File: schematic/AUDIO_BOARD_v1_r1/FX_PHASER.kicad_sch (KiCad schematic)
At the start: 43 parts, among them U50 LM13700, U51 LM13700, U52 OPA1678, U53 OPA1678, U54 OPA1678

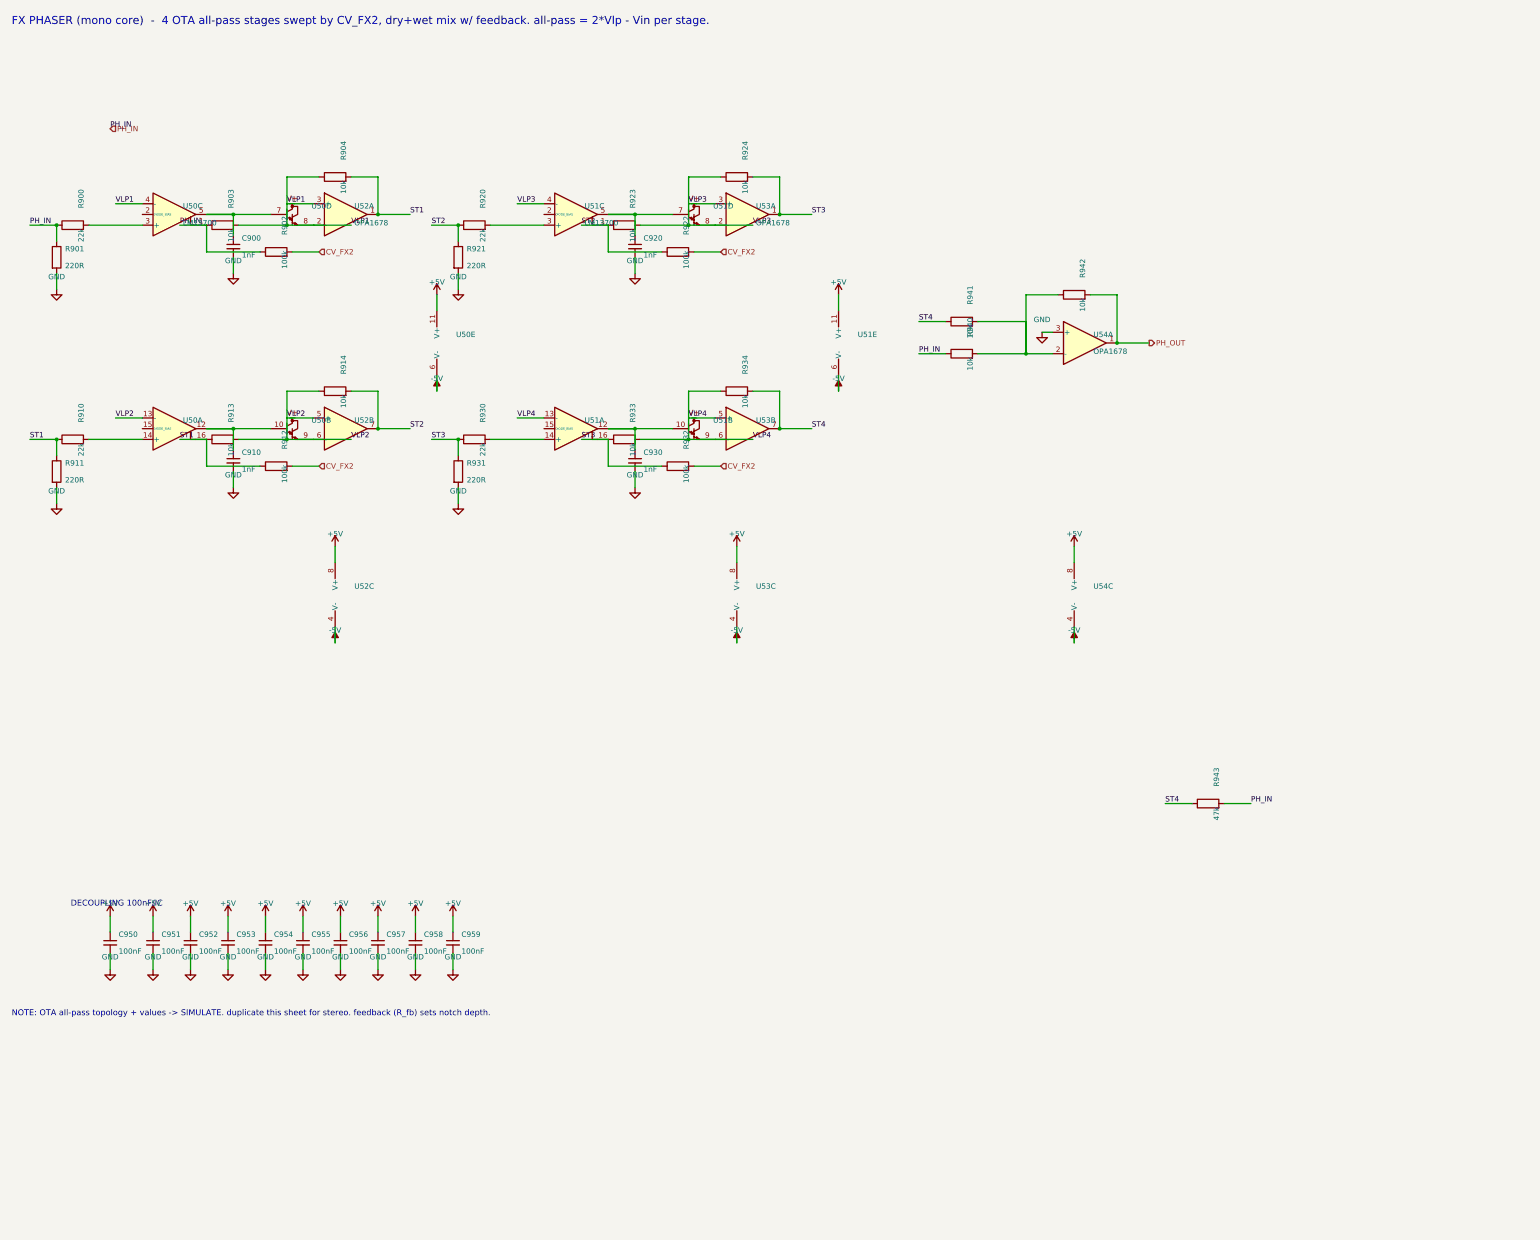
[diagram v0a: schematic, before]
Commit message: readme, audio board schematic stuff
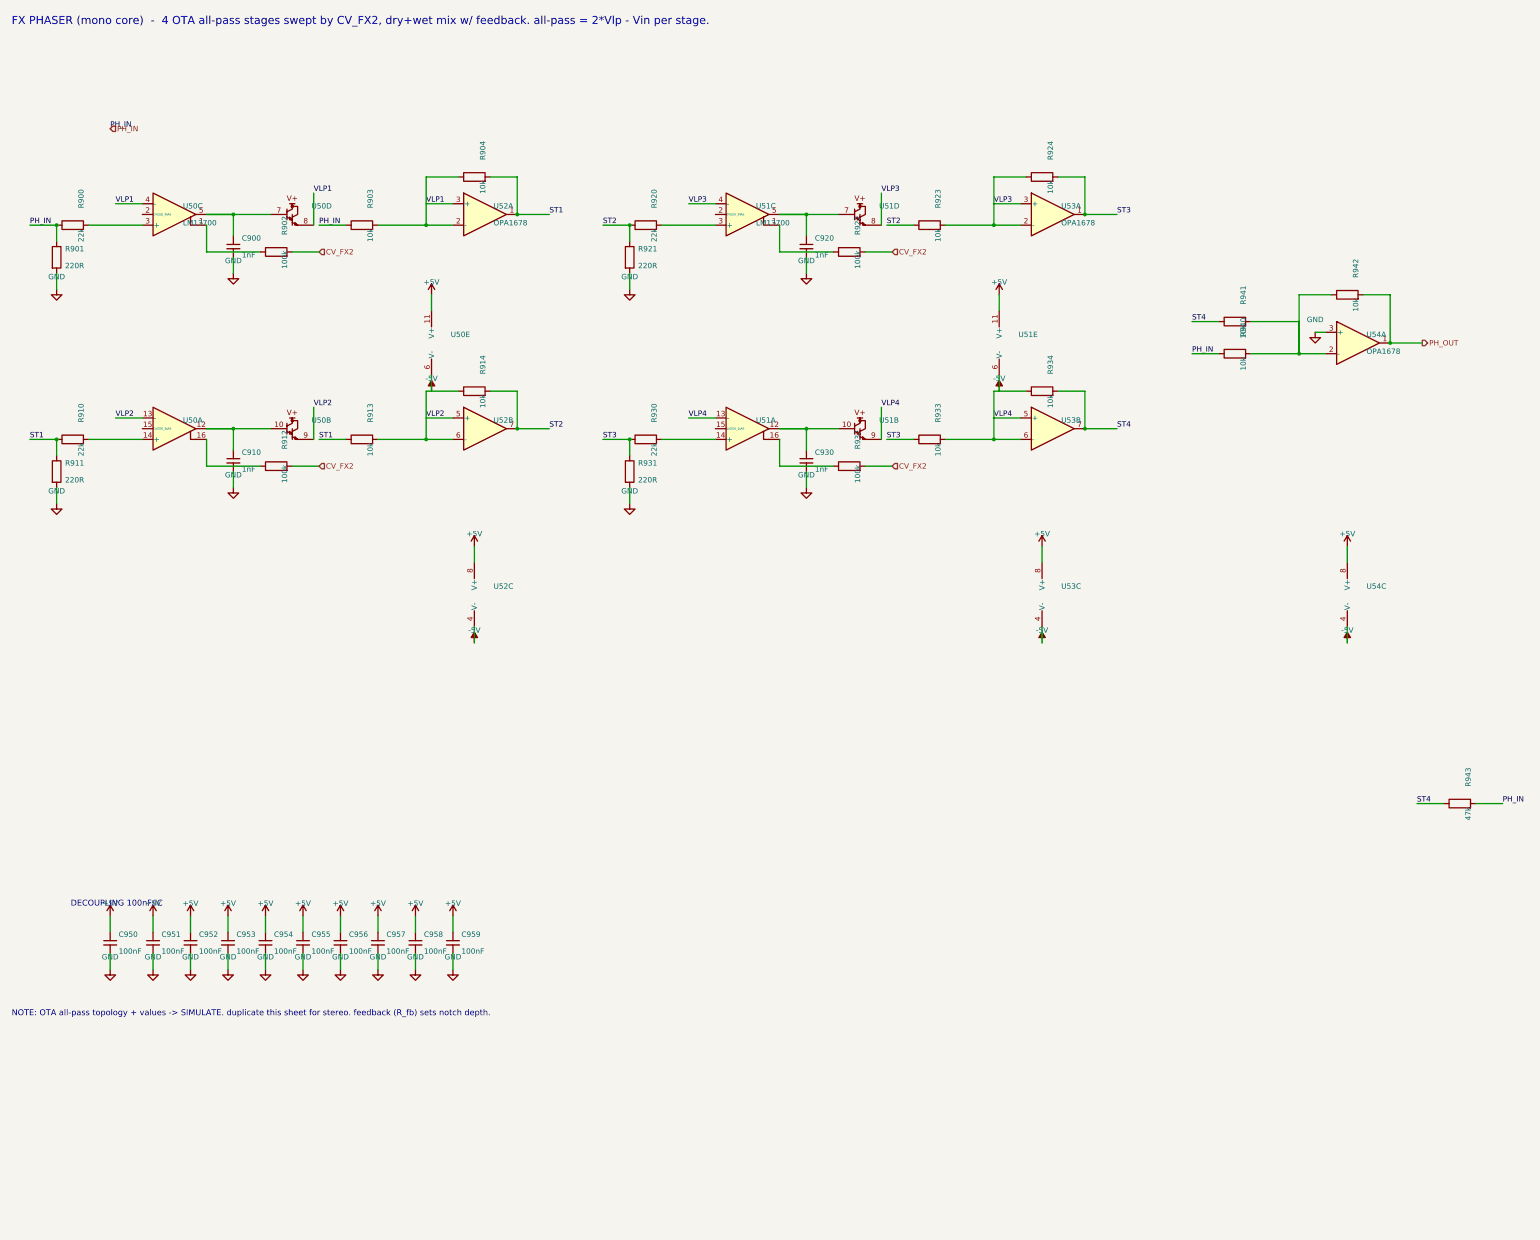
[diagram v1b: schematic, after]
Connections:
- net PH_IN: no longer R902.1, U50.1
- net ST1: no longer R912.1, U50.16
- net ST2: no longer R922.1, U51.1
- net ST3: no longer R932.1, U51.16
- new net: R902.1, U50.1
- new net: R912.1, U50.16
- new net: R932.1, U51.16
- new net: R922.1, U51.1

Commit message: phaser? schematic is messy
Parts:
- removed C900, C920: 1nF, Capacitor_SMD:C_0402_1005Metric, symbol Device:C_Small
- removed C950, C951, C952, C953, C954, C955, C956, C957, C958, C959: 100nF, Capacitor_SMD:C_0402_1005Metric, symbol Device:C_Small
- removed R900, R910, R930: 22k, Resistor_SMD:R_0402_1005Metric, symbol Device:R
- removed R904, R942: 10k, Resistor_SMD:R_0402_1005Metric, symbol Device:R
- removed R922: 100k, Resistor_SMD:R_0402_1005Metric, symbol Device:R
- removed U52, U53: OPA1678, Package_DIP:DIP-8_W7.62mm_SMDSocket_SmallPads, symbol Amplifier_Operational:OPA1678
- added C904, C916, C922, C936, C942, C948: 1nF, Capacitor_SMD:C_0402_1005Metric, symbol Device:C_Small
- added C980, C981, C982, C983, C984, C985, C986, C987, C988, C989, C990: 100nF, Capacitor_SMD:C_0402_1005Metric, symbol Device:C_Small
- added R905, R906, R917, R918, R937, R938, R944, R949, R950: 10k, Resistor_SMD:R_0402_1005Metric, symbol Device:R
- added R907, R919, R927, R939, R945, R953, R954, R955, R956, R957, R958: 22k, Resistor_SMD:R_0402_1005Metric, symbol Device:R
- added R908, R928, R946: 220R, Resistor_SMD:R_0402_1005Metric, symbol Device:R
- added R909, R915, R925, R929, R935, R947, R951: 100k, Resistor_SMD:R_0402_1005Metric, symbol Device:R
- added R926, R952: 47k, Resistor_SMD:R_0402_1005Metric, symbol Device:R
- added unit 2 of U54
- added U55, U61: OPA1678, symbol Amplifier_Operational:OPA1678
- added U57, U58: LM13700, symbol Amplifier_Operational:LM13700
- added U60, U62: OPA1678, Package_DIP:DIP-8_W7.62mm_SMDSocket_SmallPads, symbol Amplifier_Operational:OPA1678
- added U63: 4053, Package_SO:SOIC-16_3.9x9.9mm_P1.27mm, symbol 4xxx:4053
- R901: value 220R -> 22k
- R902: value 100k -> 220R
- R903, R941: value 10k -> 100k
- R911, R931: value 220R -> 10k
- R912, R932: value 100k -> 10k
- R913, R933: value 10k -> 22k
- R914, R934, R940: value 10k -> 220R
- R920: value 22k -> 220R
- R921: value 220R -> 100k
- R943: value 47k -> 10k
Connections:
- net +5V: now also C980.1, C982.1, C984.1, C986.1, C988.1, C990.1, U55.8 (V+), U57.11 (V+), U58.11 (V+), U60.8 (V+), U61.8 (V+), U62.8 (V+), U63.16 (VDD)
- net -5V: now also C981.1, C983.1, C985.1, C987.1, C989.1, U55.4 (V-), U57.6 (V-), U58.6 (V-), U60.4 (V-), U61.4 (V-), U62.4 (V-), U63.7 (VEE)
- net CV_FX2: now also R903.1, R921.1, R941.1, R909.1, R915.1, R929.1, R935.1, R947.1; no longer R902.2, R912.2, R932.2
- net GND: now also R902.2, R914.2, R920.2, R934.2, R940.2, C904.2, C916.2, C922.2, C936.2, C942.2, C948.2, C980.2, C981.2, C982.2, C983.2, C984.2, C985.2, C986.2, C987.2, C988.2, C989.2, C990.2, R908.2, R928.2, R946.2, U62.3 (+), U62.5 (+), U63.6 (Inh), U63.8 (VSS), U63.9 (C); no longer R901.2, R911.2, R921.2, R931.2, U54.3 (+)
- net OO_L1: now reaches U50.5, U50.7
- net OO_L1: now also C904.1
- net ATT_L1: now reaches U50.3 (+)
- net ATT_L1: now also R901.2, R902.1
- net IAB_L1: now reaches U50.1
- net IAB_L1: now also R903.2; no longer R902.1
- net ATT_L4: now reaches U51.14 (+)
- net ATT_L4: now also R920.1, R919.2
- net OO_L4: now reaches U51.10, U51.12
- net OO_L4: now also C922.1; no longer C930.1
- net AP2_L: now reaches R912.1
- net AP2_L: now also R913.1, R917.1, U54.7; no longer U50.16
- net AP1_R: now reaches R932.1
- net AP1_R: now also R933.1, R937.1, U60.1; no longer U51.16
- net IAB_L3: now reaches U51.1
- net IAB_L3: now also R915.2
- net ATT_L3: now reaches U51.3 (+)
- net ATT_L3: now also R913.2, R914.1; no longer R920.2
- net OO_L3: now reaches U51.5, U51.7
- net OO_L3: now also C916.1
- net OO_L2: now reaches C910.1, U50.10, U50.12
- net ATT_L2: now reaches U50.14 (+)
- net ATT_L2: now also R907.2, R908.1
- removed net PH_IN: R901.1, R903.1, R940.1, R943.2
- net PH_OUT renamed AP1_L
- net AP1_L: now also R911.1, R906.1, R907.1
- removed net ST1: R911.1, R913.1
- removed net ST2: R914.2, R920.1, R921.1, R923.1
- removed net ST3: R924.2, R931.1, R933.1
- removed net ST4: R934.2, R941.1, R943.1
- net VLP1 renamed VLP_L1
- net VLP_L1: now also U54.3 (+); no longer R903.2
- net VLP2 renamed VLP_L2
- net VLP_L2: now also U54.5 (+); no longer R913.2, R914.1
- net VLP3 renamed VLP_L3
- net VLP_L3: now also U55.3 (+); no longer R923.2, R924.1
- net VLP4 renamed ATT_R2
- net ATT_R2: now also U57.14 (+); no longer U51.13 (-), U51.9
- new net AP2_R: R938.1, R939.1, R943.1, U60.7
- new net AP3_L: R918.1, R919.1, R923.1, U55.1
- new net AP3_R: R944.1, R945.1, R949.1, U61.1
- new net AP4_L: R924.1, R926.1, R954.1, U55.7
- new net AP4_R: R950.1, R952.1, R957.1, U61.7
- new net ATT_R1: R927.2, R928.1, U57.3 (+)
- new net ATT_R3: R939.2, R940.1, U58.3 (+)
- new net ATT_R4: R945.2, R946.1, U58.14 (+)
- new net DN_L1: R905.2, R906.2, U54.2 (-)
- new net DN_L2: R911.2, R912.2, U54.6 (-)
- new net DN_L3: R917.2, R918.2, U55.2 (-)
- new net DN_L4: R923.2, R924.2, U55.6 (-)
- new net DN_R1: R931.2, R932.2, U60.2 (-)
- new net DN_R2: R937.2, R938.2, U60.6 (-)
- new net DN_R3: R943.2, R944.2, U61.2 (-)
- new net DN_R4: R949.2, R950.2, U61.6 (-)
- new net FX_EN2: U63.10 (B), U63.11 (A)
- new net IAB_L2: R909.2, U50.16
- new net IAB_L4: R921.2, U51.16
- new net IAB_R1: R929.2, U57.1
- new net IAB_R2: R935.2, U57.16
- new net IAB_R3: R941.2, U58.1
- new net IAB_R4: R947.2, U58.16
- new net MN_L: R953.2, R954.2, R955.2, U62.2 (-)
- new net MN_R: R956.2, R957.2, R958.2, U62.6 (-)
- new net OO_R1: C930.1, U57.5, U57.7
- new net OO_R2: C936.1, U57.10, U57.12
- new net OO_R3: C942.1, U58.5, U58.7
- new net OO_R4: C948.1, U58.10, U58.12
- new net PH_L_IN: R925.1, R953.1, U63.12 (X0)
- new net PH_L_OUT: U63.14 (X)
- new net PH_R_IN: R951.1, R956.1, U63.2 (Y0)
- new net PH_R_OUT: U63.15 (Y)
- new net S1_L: R901.1, R905.1, R925.2, R926.2
- new net S1_R: R927.1, R931.1, R951.2, R952.2
- new net VLP_L4: U51.13 (-), U51.9, U55.5 (+)
- new net VLP_R1: U57.4 (-), U57.8, U60.3 (+)
- new net VLP_R2: U57.13 (-), U57.9, U60.5 (+)
- new net VLP_R3: U58.4 (-), U58.8, U61.3 (+)
- new net VLP_R4: U58.13 (-), U58.9, U61.5 (+)
- new net WET_L: R955.1, U62.1, U63.13 (X1)
- new net WET_R: R958.1, U62.7, U63.1 (Y1)
- no-connect marks 0 -> 11
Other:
- note added: "FX PHASER (true stereo) - 4 OTA all-pass stages/channel swept by CV_FX2 (STM32 LFO); feedback for notch depth; dry+wet mix; bypass via CD4053 on FX_EN2."
- note added: "PHASER CHANNEL L"
- note added: "PHASER CHANNEL R"
- note added: "all-pass stage = OTA-C lowpass (Vlp) + diff amp (2*Vlp - Vin). NOTE: connectivity + topology verified; LEVELS/OTA-bias need real-LM13700-model sim before fab."
- note removed: "FX PHASER (mono core) - 4 OTA all-pass stages swept by CV_FX2, dry+wet mix w/ feedback. all-pass = 2*Vlp - Vin per stage."
- note removed: "NOTE: OTA all-pass topology + values -> SIMULATE. duplicate this sheet for stereo. feedback (R_fb) sets notch depth."

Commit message: sim, render, audio stuff
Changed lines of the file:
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@@
 		(instances (project "AUDIO_BOARD" (path "/ba93534c-f2e3-4dc0-9a76-585fdc68cf39/aa11bb22-cc33-dd44-ee55-ff6677889900" (reference "R903") (unit 1)))))
 	(wire (pts (xy 69.85 250.19) (xy 66.04 250.19)) (stroke (width 0) (type default)))
-	(label "CV_FX2" (at 66.04 250.19 0) (effects (font (size 1.27 1.27)) (justify left bottom)))
+	(hierarchical_label "CV_FX2" (shape input) (at 66.04 250.19 0) (effects (font (size 1.27 1.27)) (justify left)))
 	(wire (pts (xy 77.47 250.19) (xy 81.28 250.19)) (stroke (width 0) (type default)))
 	(label "IAB_L1" (at 81.28 250.19 0) (effects (font (size 1.27 1.27)) (justify left bottom)))
@@
 		(instances (project "AUDIO_BOARD" (path "/ba93534c-f2e3-4dc0-9a76-585fdc68cf39/aa11bb22-cc33-dd44-ee55-ff6677889900" (reference "R925") (unit 1)))))
 	(wire (pts (xy 201.93 264.16) (xy 198.12 264.16)) (stroke (width 0) (type default)))
-	(label "PH_L_IN" (at 198.12 264.16 0) (effects (font (size 1.27 1.27)) (justify left bottom)))
+	(hierarchical_label "PH_L_IN" (shape input) (at 198.12 264.16 0) (effects (font (size 1.27 1.27)) (justify left)))
 	(wire (pts (xy 209.55 264.16) (xy 213.36 264.16)) (stroke (width 0) (type default)))
 	(label "S1_L" (at 213.36 264.16 0) (effects (font (size 1.27 1.27)) (justify left bottom)))
@@
 		(instances (project "AUDIO_BOARD" (path "/ba93534c-f2e3-4dc0-9a76-585fdc68cf39/aa11bb22-cc33-dd44-ee55-ff6677889900" (reference "R951") (unit 1)))))
 	(wire (pts (xy 69.85 292.1) (xy 66.04 292.1)) (stroke (width 0) (type default)))
-	(label "PH_R_IN" (at 66.04 292.1 0) (effects (font (size 1.27 1.27)) (justify left bottom)))
+	(hierarchical_label "PH_R_IN" (shape input) (at 66.04 292.1 0) (effects (font (size 1.27 1.27)) (justify left)))
 	(wire (pts (xy 77.47 292.1) (xy 81.28 292.1)) (stroke (width 0) (type default)))
 	(label "S1_R" (at 81.28 292.1 0) (effects (font (size 1.27 1.27)) (justify left bottom)))
@@
 	(hierarchical_label "PH_L_OUT" (shape output) (at 339.09 194.31 0) (effects (font (size 1.27 1.27)) (justify left)))
 	(wire (pts (xy 307.34 219.71) (xy 299.72 219.71)) (stroke (width 0) (type default)))
-	(label "FX_EN2" (at 299.72 219.71 0) (effects (font (size 1.27 1.27)) (justify left bottom)))
+	(hierarchical_label "FX_EN2" (shape input) (at 299.72 219.71 0) (effects (font (size 1.27 1.27)) (justify left)))
 	(wire (pts (xy 307.34 201.93) (xy 300.99 201.93)) (stroke (width 0) (type default)))
 	(label "PH_R_IN" (at 300.99 201.93 0) (effects (font (size 1.27 1.27)) (justify left bottom)))
@@
 		(property "Value" "-5V" (at 326.39 233.22 0) (effects (font (size 1.27 1.27))))
 		(instances (project "AUDIO_BOARD" (path "/ba93534c-f2e3-4dc0-9a76-585fdc68cf39/aa11bb22-cc33-dd44-ee55-ff6677889900" (reference "#PWR939") (unit 1)))))
-	(hierarchical_label "PH_L_IN" (shape input) (at 24.13 39.37 0) (effects (font (size 1.27 1.27)) (justify left)))
-	(label "PH_L_IN" (at 24.13 39.37 0) (effects (font (size 1.27 1.27)) (justify left bottom)))
-	(hierarchical_label "PH_R_IN" (shape input) (at 24.13 129.54 0) (effects (font (size 1.27 1.27)) (justify left)))
-	(label "PH_R_IN" (at 24.13 129.54 0) (effects (font (size 1.27 1.27)) (justify left bottom)))
-	(hierarchical_label "CV_FX2" (shape input) (at 24.13 199.39 0) (effects (font (size 1.27 1.27)) (justify left)))
-	(label "CV_FX2" (at 24.13 199.39 0) (effects (font (size 1.27 1.27)) (justify left bottom)))
-	(hierarchical_label "FX_EN2" (shape input) (at 24.13 209.55 0) (effects (font (size 1.27 1.27)) (justify left)))
-	(label "FX_EN2" (at 24.13 209.55 0) (effects (font (size 1.27 1.27)) (justify left bottom)))
 	(text "DECOUPLING 100nF/IC" (exclude_from_sim no) (at 30 286 0) (effects (font (size 1.4 1.4) ) (justify left bottom)))
 	(symbol (lib_id "Device:C_Small") (at 39.37 292.1 0) (unit 1)
@@
 	(no_connect
 		(at 22.86 39.37)
+		(uuid "dbFX0000-0000-0000-0000-000000000000")
 	)
 	(no_connect
 		(at 22.86 129.54)
+		(uuid "dbFX0000-0000-0000-0000-000000000001")
 	)
 	(no_connect
 		(at 102.87 39.37)
+		(uuid "dbFX0000-0000-0000-0000-000000000002")
 	)
 	(no_connect
 		(at 102.87 129.54)
+		(uuid "dbFX0000-0000-0000-0000-000000000003")
 	)
 	(no_connect
 		(at 182.88 39.37)
+		(uuid "dbFX0000-0000-0000-0000-000000000004")
 	)
 	(no_connect
 		(at 182.88 129.54)
+		(uuid "dbFX0000-0000-0000-0000-000000000005")
 	)
 	(no_connect
 		(at 262.89 39.37)
+		(uuid "dbFX0000-0000-0000-0000-000000000006")
 	)
 	(no_connect
 		(at 262.89 129.54)
+		(uuid "dbFX0000-0000-0000-0000-000000000007")
 	)
 	(no_connect
 		(at 307.34 209.55)
+		(uuid "dbFX0000-0000-0000-0000-000000000008")
 	)
 	(no_connect
 		(at 307.34 212.09)
+		(uuid "dbFX0000-0000-0000-0000-000000000009")
 	)
 	(no_connect
 		(at 332.74 209.55)
+		(uuid "dbFX0000-0000-0000-0000-000000000010")
 	)
 )
